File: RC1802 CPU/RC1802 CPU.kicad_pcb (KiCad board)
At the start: 2 copper layers, 99.1 x 99.1 mm, 49 parts, among them J1 Mount, J2 Mount, J3 Mount, J4 Mount, J5 CONN_01X39, J6 CONN_02X20, J7 BARREL_JACK, J8 Conn_01x05, U1 74LS04, U2 CDP1802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

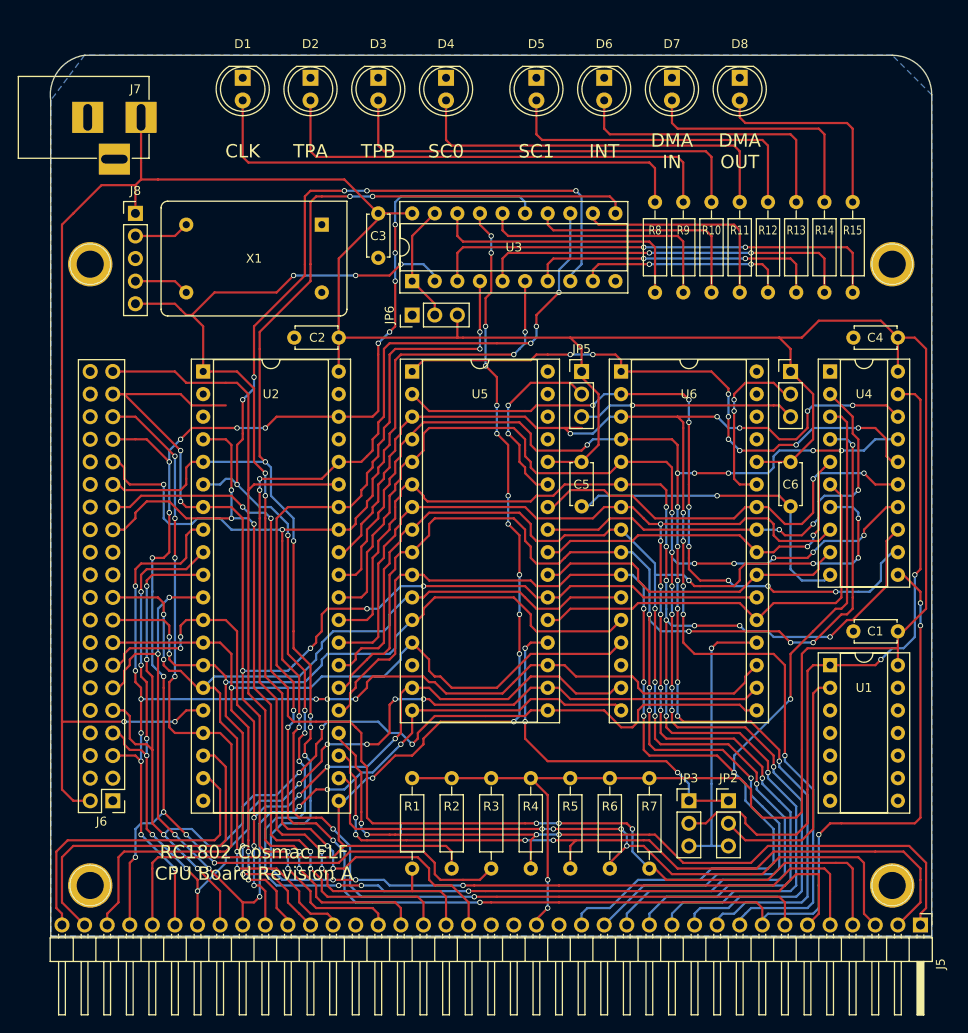
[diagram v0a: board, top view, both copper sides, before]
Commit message: Fixed stupid socket pin count mistake
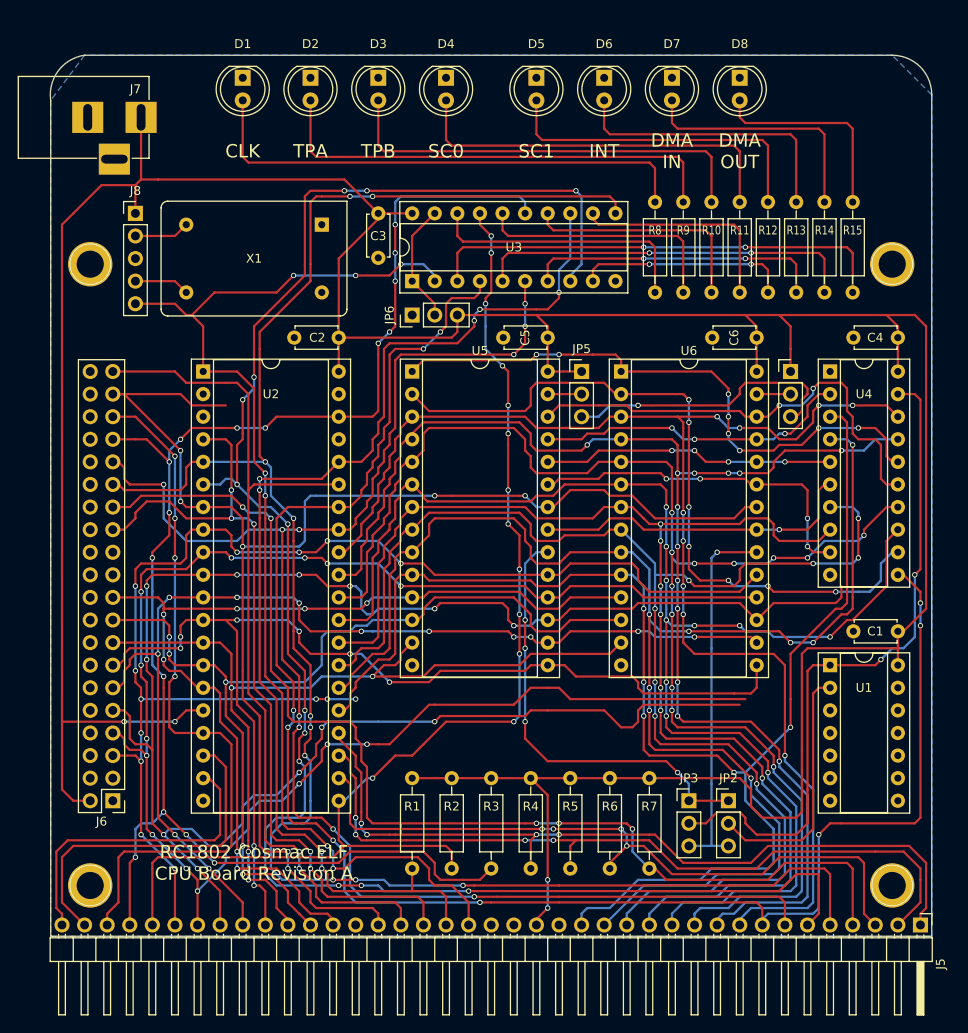
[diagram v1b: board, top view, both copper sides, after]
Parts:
- U5, U6: footprint Housings_DIP:DIP-32_W15.24mm_Socket -> Housings_DIP:DIP-28_W15.24mm_Socket
- moved C5 14.5 mm to (156.2, 80.0), turned to 180 degrees
- moved C6 14.5 mm to (179.7, 80.0), turned to 180 degrees
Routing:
- net /BUS5: track 138.5 -> 215.1 mm, vias 7 -> 12
- net /BUS6: track 133.6 -> 194.9 mm, vias 12 -> 14
- net GND: track 36.8 -> 0.00 mm, vias 1 -> 0
- net /BUS7: track 132.4 -> 149.9 mm, vias 10 -> 14
- net Net-(JP5-Pad2): track 21.3 -> 3.81 mm, vias 2 -> 0
- net /BUS3: track 105.7 -> 121.8 mm
- net Net-(JP4-Pad2): track 19.7 -> 3.81 mm, vias 2 -> 0
- net /MA8: track 51.6 -> 35.7 mm
- net /MA10: track 48.9 -> 36.8 mm, vias 0 -> 1
- net VCC: track 402.2 -> 390.6 mm
- net SLOT2_CS: track 32.0 -> 42.2 mm
- net SLOT1_CS: track 39.8 -> 49.6 mm, vias 3 -> 4
- net /MA9: track 41.6 -> 32.8 mm, vias 2 -> 4
- net /BUS4: track 111.7 -> 119.4 mm, vias 8 -> 12
- net ~WE: track 24.5 -> 31.9 mm
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
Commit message: Tidying up leftover segments
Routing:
- net /BUS5: track 215.1 -> 125.9 mm, vias 12 -> 9
- net /BUS6: track 194.9 -> 120.7 mm, vias 14 -> 10
- net /BUS7: track 149.9 -> 125.7 mm, vias 14 -> 10
- net MRD: track 160.1 -> 146.9 mm
- net /MA2: track 153.4 -> 147.5 mm, vias 8 -> 5
- net /BUS3: track 121.8 -> 117.3 mm, vias 8 -> 10
- net /BUS2: track 100.4 -> 96.5 mm
- net TPB: track 174.8 -> 171.1 mm, vias 10 -> 9
- net /BUS4: track 119.4 -> 122.2 mm
- net EF1: track 90.5 -> 92.2 mm, vias 4 -> 2
- net DMA_OUT: track 132.1 -> 133.6 mm
- net (no net): track 1.27 -> 0.00 mm
- net /MA5: track 158.6 -> 159.7 mm, vias 12 -> 10
- net EF2: track 87.5 -> 88.6 mm
- net SC1: track 209.9 -> 209.0 mm
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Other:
- board text added: "BUS LATCH"
- board text added: "RC1802 Cosmac ELF CPU Board Revision B"
- board text added: "Status Enable"
- board text removed: "LATCH"
- board text removed: "RC1802 Cosmac ELF CPU Board Revision A"

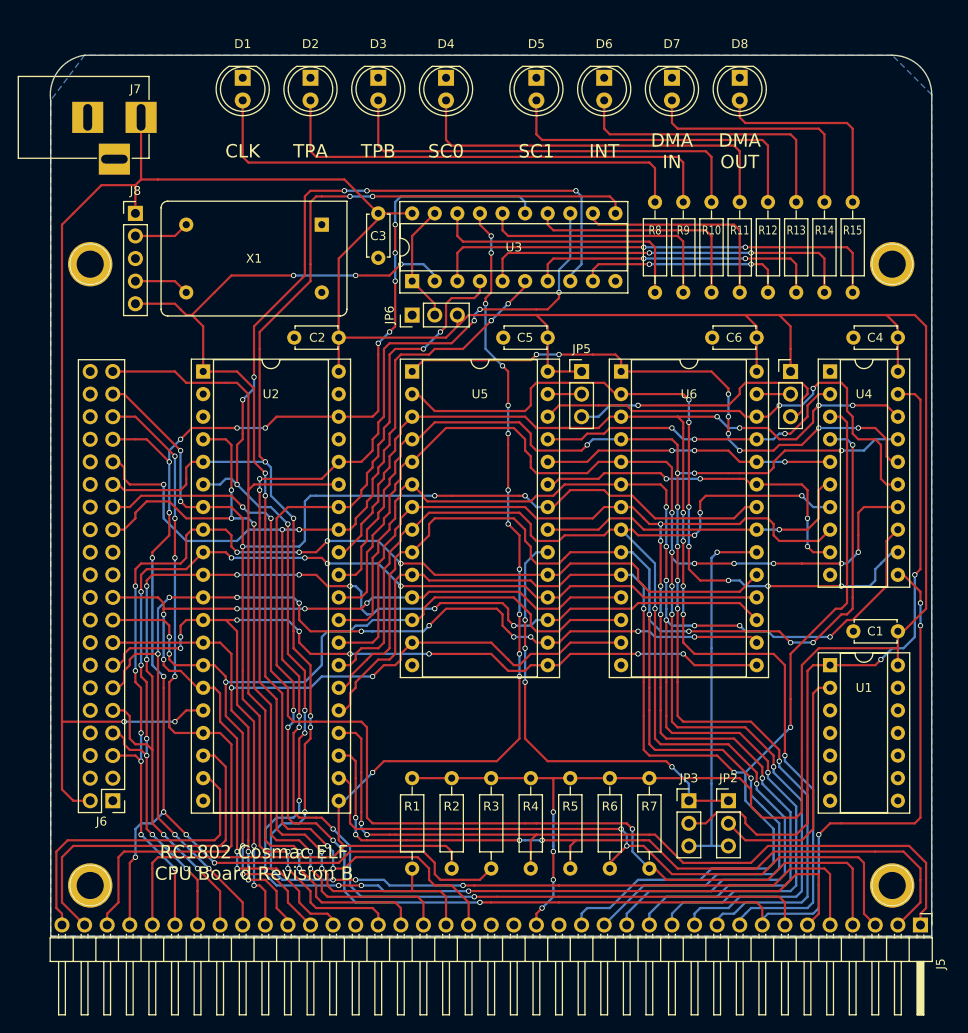
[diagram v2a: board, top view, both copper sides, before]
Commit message: Added Q connector and some silksceen info
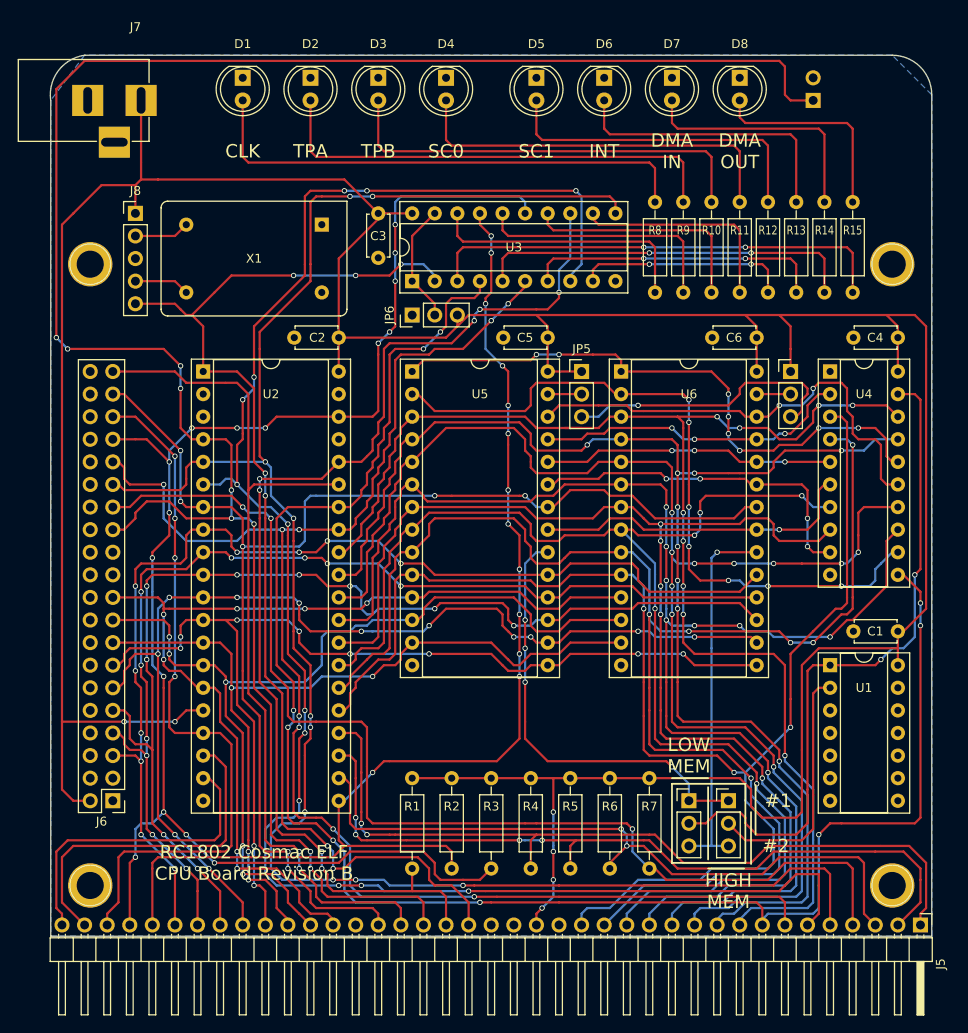
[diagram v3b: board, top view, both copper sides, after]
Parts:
- added J9: Conn_Q, Pin_Headers:Pin_Header_Angled_1x02_Pitch2.54mm, B.Cu at (186.1, 53.3)
- J8: value Conn_01x05 -> Conn_CLK
- moved J7 1.90 mm to (110.5, 53.3)
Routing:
- net Q: track 90.7 -> 234.1 mm, vias 5 -> 9
- net VCC: track 390.1 -> 392.0 mm
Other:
- board text added: "#1"
- board text added: "#2"
- board text added: "5v DC"
- board text added: "Q"

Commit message: Q connector now 4 pins to match speaker and TTL serial
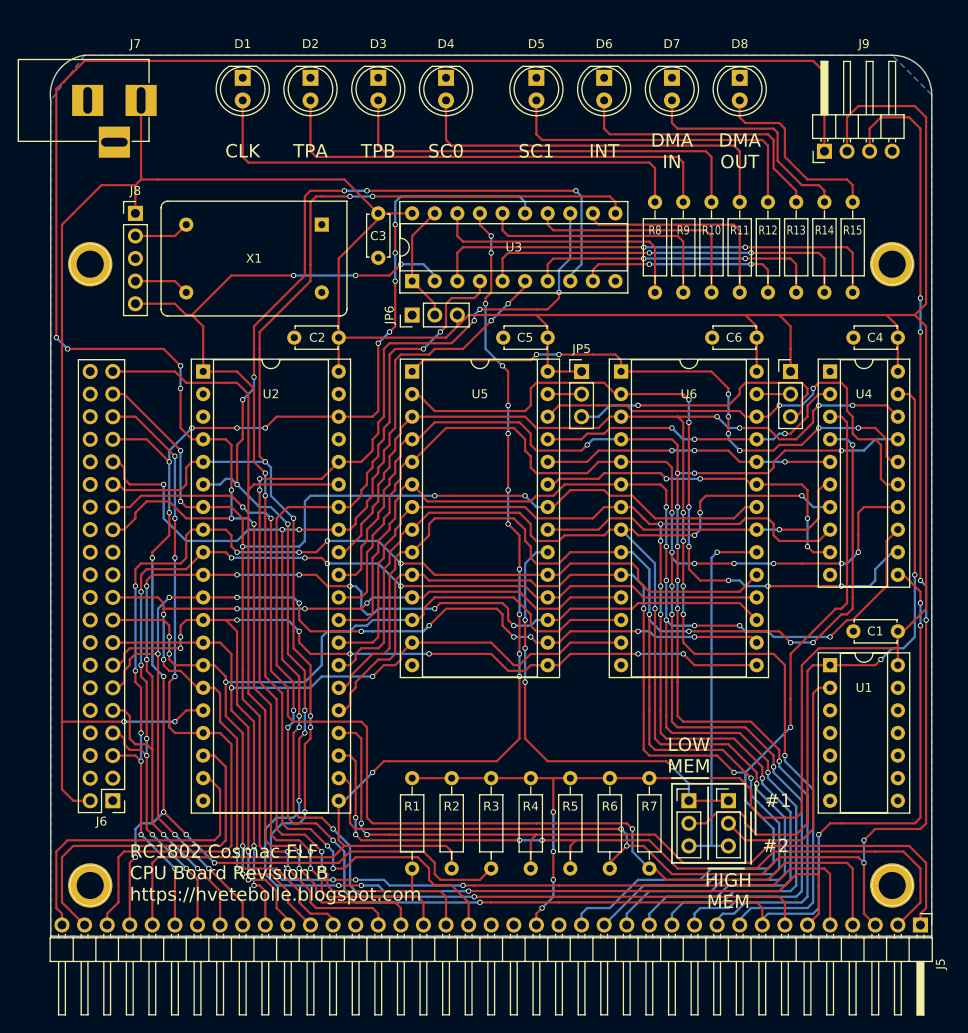
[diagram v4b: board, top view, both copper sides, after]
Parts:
- J9: footprint Pin_Headers:Pin_Header_Angled_1x02_Pitch2.54mm -> Pin_Headers:Pin_Header_Angled_1x04_Pitch2.54mm; moved to F.Cu
- moved J9 5.85 mm to (187.3, 59.1), turned to 90 degrees
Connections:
- J9 pad 2: GND -> VCC
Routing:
- net EF3: track 78.8 -> 176.8 mm, vias 2 -> 8
- net VCC: track 392.0 -> 428.5 mm
- net Q: track 234.1 -> 241.1 mm
- net Net-(D8-Pad2): track 23.4 -> 21.5 mm
- net Net-(D7-Pad2): track 27.8 -> 26.0 mm
- net Net-(D6-Pad2): track 32.3 -> 30.8 mm
- net /MA15: track 76.3 -> 75.4 mm
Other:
- board text added: "EF3"
- board text added: "RC1802 Cosmac ELF CPU Board Revision B https://hvetebolle.blogspot.com"
- board text added: "VCC"
- board text removed: "RC1802 Cosmac ELF CPU Board Revision B"

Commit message: Flipped oscillator, silkscreen cleanup
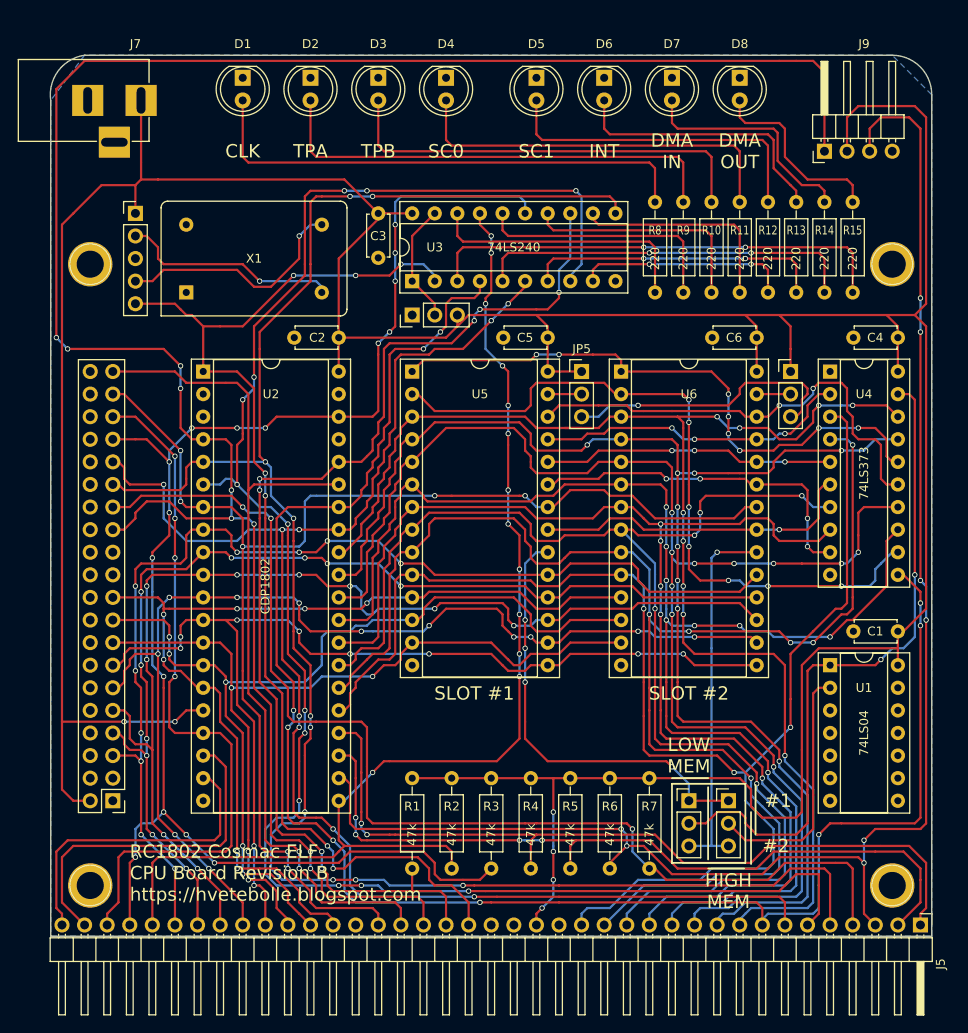
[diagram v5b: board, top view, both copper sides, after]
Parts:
- moved X1 17.0 mm to (115.6, 74.9), turned to 0 degrees
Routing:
- net Net-(J8-Pad4): track 6.24 -> 26.7 mm, vias 0 -> 1
- net Net-(J8-Pad2): track 6.24 -> 24.7 mm, vias 0 -> 1
- net CLOCK: track 131.4 -> 130.6 mm

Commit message: Accidentally swapped VCC and GND on oscillator, no wonder it didn't work :-(
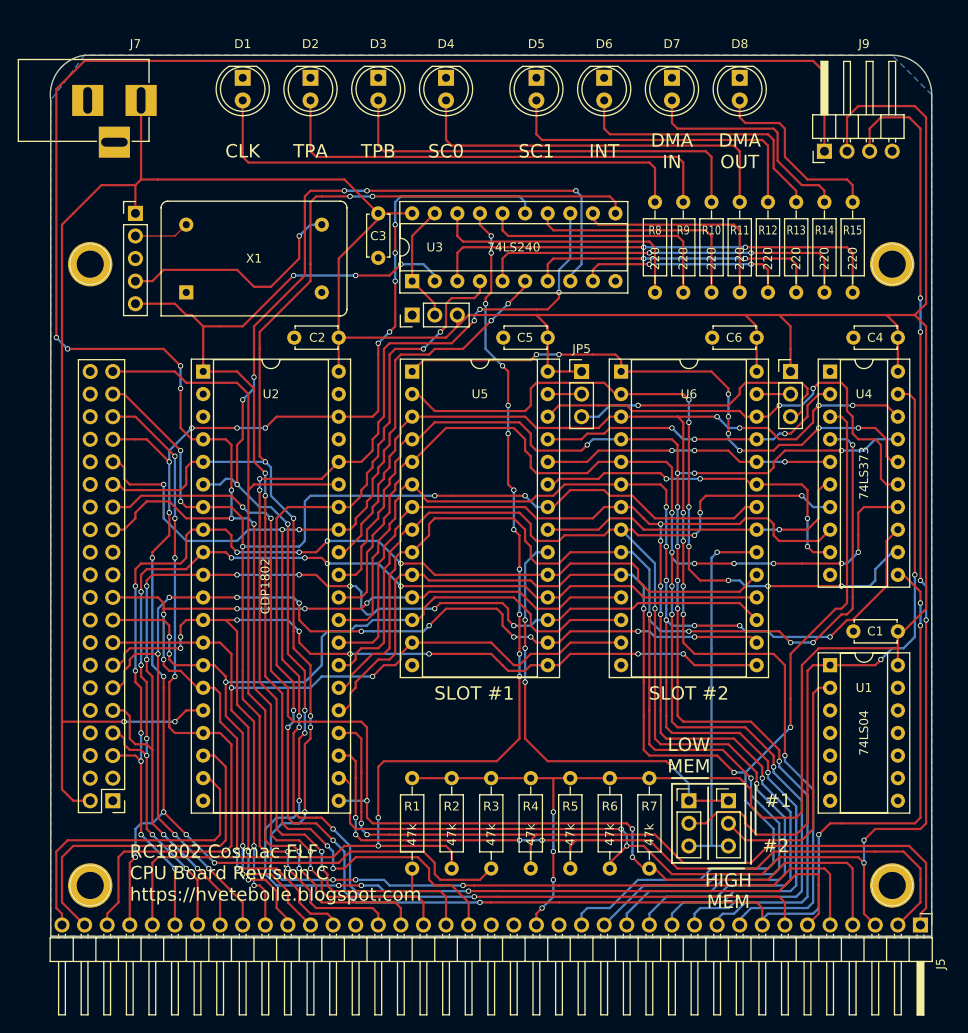
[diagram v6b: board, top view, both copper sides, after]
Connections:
- U2 pad 21: DMA_OUT -> EF4
- X1 pad 14: GND -> Net-(J8-Pad2)
- X1 pad 7: Net-(J8-Pad2) -> GND
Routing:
- net Net-(J8-Pad2): track 24.7 -> 6.24 mm, vias 1 -> 0
- net EF4: track 128.3 -> 132.5 mm, vias 3 -> 5
- net DMA_OUT: track 133.6 -> 131.1 mm, vias 13 -> 14
- net GND: track 0.00 -> 0.64 mm
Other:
- board text added: "RC1802 Cosmac ELF CPU Board Revision C https://hvetebolle.blogspot.com"
- board text removed: "RC1802 Cosmac ELF CPU Board Revision B https://hvetebolle.blogspot.com"
